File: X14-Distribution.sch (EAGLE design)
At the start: 57 parts, among them J2 PESC-02-12-02-01-X-VT-LC(DIST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, Q1 310mA/60V/1.6Ω, Q2 IRF1018EPBF, Q3 IRF1018EPBF, Q4 IRF1018EPBF, Q5 IRLML5203, Q6 IRLML5203, Q7 IRLML5203, Q8 IRLML5203, U1 DIST_OR_CONTROL_ALTMK06A-M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

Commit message: Made some more changes to the board
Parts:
- renumbered J2 to BRICKS2
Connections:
- net +12V: no longer D13.C, D14.C
- net +12V_A: now also D13.C
- net +12V_B: now also D14.C
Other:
- moved on the sheet: D13, D14
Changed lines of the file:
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@@
 <part name="CONVERSION" library="CONN, Distribution-Conversion" deviceset="DISTRIBUTION-CONVERSION" device=""/>
 <part name="BRICKS1" library="CONN, Distribution-Bricks" deviceset="PESC-02-12-02-01-X-VT-LC(DISTRIBUTION-BRICKS)" device=""/>
-<part name="J2" library="CONN, Distribution-Bricks" deviceset="PESC-02-12-02-01-X-VT-LC(DISTRIBUTION-BRICKS)" device=""/>
+<part name="BRICKS2" library="CONN, Distribution-Bricks" deviceset="PESC-02-12-02-01-X-VT-LC(DISTRIBUTION-BRICKS)" device=""/>
 <part name="D13" library="SparkFun-DiscreteSemi" library_urn="urn:adsk.eagle:library:514" deviceset="DIODE-ZENER" device="-DZ2J150M0L" package3d_urn="urn:adsk.eagle:package:38444/1" value="18V"/>
 <part name="D14" library="SparkFun-DiscreteSemi" library_urn="urn:adsk.eagle:library:514" deviceset="DIODE-ZENER" device="-DZ2J150M0L" package3d_urn="urn:adsk.eagle:package:38444/1" value="18V"/>
@@
 <attribute name="VALUE" x="76.2" y="-158.496" size="1.778" layer="96"/>
 </instance>
-<instance part="J2" gate="G$1" x="181.864" y="-140.208" smashed="yes">
+<instance part="BRICKS2" gate="G$1" x="181.864" y="-140.208" smashed="yes">
 <attribute name="NAME" x="169.164" y="-124.46" size="1.778" layer="95"/>
 <attribute name="VALUE" x="169.164" y="-157.988" size="1.778" layer="96"/>
 </instance>
-<instance part="D13" gate="G$1" x="67.564" y="133.604" smashed="yes" rot="R90">
-<attribute name="NAME" x="65.532" y="131.064" size="1.778" layer="95" font="vector" rot="R90"/>
-<attribute name="VALUE" x="69.596" y="131.064" size="1.778" layer="96" font="vector" rot="R90" align="top-left"/>
-</instance>
-<instance part="D14" gate="G$1" x="67.818" y="77.216" smashed="yes" rot="R90">
-<attribute name="NAME" x="65.786" y="74.676" size="1.778" layer="95" font="vector" rot="R90"/>
-<attribute name="VALUE" x="69.85" y="74.676" size="1.778" layer="96" font="vector" rot="R90" align="top-left"/>
+<instance part="D13" gate="G$1" x="30.988" y="136.144" smashed="yes" rot="R90">
+<attribute name="NAME" x="28.956" y="133.604" size="1.778" layer="95" font="vector" rot="R90"/>
+<attribute name="VALUE" x="33.02" y="133.604" size="1.778" layer="96" font="vector" rot="R90" align="top-left"/>
+</instance>
+<instance part="D14" gate="G$1" x="30.988" y="80.264" smashed="yes" rot="R90">
+<attribute name="NAME" x="28.956" y="77.724" size="1.778" layer="95" font="vector" rot="R90"/>
+<attribute name="VALUE" x="33.02" y="77.724" size="1.778" layer="96" font="vector" rot="R90" align="top-left"/>
 </instance>
 </instances>
@@
 <wire x1="164.084" y1="-150.368" x2="154.432" y2="-150.368" width="0.1524" layer="91"/>
 <label x="154.432" y="-150.368" size="1.778" layer="95" rot="R180" xref="yes"/>
-<pinref part="J2" gate="G$1" pin="48V_GND"/>
+<pinref part="BRICKS2" gate="G$1" pin="48V_GND"/>
 </segment>
 </net>
@@
 <wire x1="164.084" y1="-145.288" x2="154.432" y2="-145.288" width="0.1524" layer="91"/>
 <label x="154.432" y="-145.288" size="1.778" layer="95" rot="R180" xref="yes"/>
-<pinref part="J2" gate="G$1" pin="48V"/>
+<pinref part="BRICKS2" gate="G$1" pin="48V"/>
 </segment>
 </net>
@@
 <wire x1="202.184" y1="-150.368" x2="212.598" y2="-150.368" width="0.1524" layer="91"/>
 <label x="212.598" y="-150.368" size="1.778" layer="95" xref="yes"/>
-<pinref part="J2" gate="G$1" pin="ON/OFF"/>
+<pinref part="BRICKS2" gate="G$1" pin="ON/OFF"/>
 </segment>
 </net>
@@
 <pinref part="U2" gate="A" pin="IN"/>
 <wire x1="36.83" y1="85.344" x2="36.83" y2="73.66" width="0.1524" layer="91"/>
-<wire x1="36.83" y1="85.344" x2="26.67" y2="85.344" width="0.1524" layer="91"/>
+<wire x1="36.83" y1="85.344" x2="30.988" y2="85.344" width="0.1524" layer="91"/>
 <junction x="36.83" y="85.344"/>
 <label x="26.67" y="85.344" size="1.778" layer="95" rot="R180" xref="yes"/>
+<pinref part="D14" gate="G$1" pin="C"/>
+<wire x1="30.988" y1="85.344" x2="26.67" y2="85.344" width="0.1524" layer="91"/>
+<wire x1="30.988" y1="82.804" x2="30.988" y2="85.344" width="0.1524" layer="91"/>
+<junction x="30.988" y="85.344"/>
 </segment>
 <segment>
@@
 <wire x1="164.084" y1="-127.508" x2="154.432" y2="-127.508" width="0.1524" layer="91"/>
 <label x="154.178" y="-127.508" size="1.778" layer="95" rot="R180" xref="yes"/>
-<pinref part="J2" gate="G$1" pin="12V"/>
+<pinref part="BRICKS2" gate="G$1" pin="12V"/>
 </segment>
 <segment>
@@
 <pinref part="Q3" gate="G$1" pin="D"/>
 <wire x1="57.15" y1="141.478" x2="52.07" y2="141.478" width="0.1524" layer="91"/>
-<wire x1="57.15" y1="141.478" x2="67.564" y2="141.478" width="0.1524" layer="91"/>
+<wire x1="57.15" y1="141.478" x2="77.47" y2="141.478" width="0.1524" layer="91"/>
 <junction x="57.15" y="141.478"/>
-<wire x1="67.564" y1="141.478" x2="77.47" y2="141.478" width="0.1524" layer="91"/>
 <wire x1="77.47" y1="141.478" x2="77.47" y2="110.49" width="0.1524" layer="91"/>
 <pinref part="C1" gate="G$1" pin="+"/>
@@
 <pinref part="Q4" gate="G$1" pin="D"/>
 <wire x1="57.15" y1="85.344" x2="52.07" y2="85.344" width="0.1524" layer="91"/>
-<wire x1="57.15" y1="85.344" x2="67.818" y2="85.344" width="0.1524" layer="91"/>
+<wire x1="57.15" y1="85.344" x2="77.47" y2="85.344" width="0.1524" layer="91"/>
 <junction x="57.15" y="85.344"/>
 <junction x="77.47" y="85.344"/>
 <pinref part="U1" gate="A" pin="VS"/>
-<wire x1="67.818" y1="85.344" x2="77.47" y2="85.344" width="0.1524" layer="91"/>
 <wire x1="77.47" y1="110.49" x2="59.69" y2="110.49" width="0.1524" layer="91"/>
 <junction x="77.47" y="110.49"/>
 <pinref part="U1" gate="A" pin="OUT"/>
 <wire x1="52.07" y1="125.73" x2="57.15" y2="125.73" width="0.1524" layer="91"/>
-<pinref part="D14" gate="G$1" pin="C"/>
-<wire x1="67.818" y1="79.756" x2="67.818" y2="85.344" width="0.1524" layer="91"/>
-<junction x="67.818" y="85.344"/>
-<pinref part="D13" gate="G$1" pin="C"/>
-<wire x1="67.564" y1="136.144" x2="67.564" y2="141.478" width="0.1524" layer="91"/>
-<junction x="67.564" y="141.478"/>
 </segment>
 <segment>
@@
 <wire x1="164.084" y1="-132.588" x2="154.686" y2="-132.588" width="0.1524" layer="91"/>
 <label x="154.432" y="-132.588" size="1.778" layer="95" rot="R180" xref="yes"/>
-<pinref part="J2" gate="G$1" pin="12V_GND"/>
+<pinref part="BRICKS2" gate="G$1" pin="12V_GND"/>
 </segment>
 <segment>
@@
 <segment>
 <pinref part="D13" gate="G$1" pin="A"/>
-<wire x1="67.564" y1="131.064" x2="67.564" y2="122.174" width="0.1524" layer="91"/>
-<label x="67.31" y="122.174" size="1.27" layer="95" rot="R180" xref="yes"/>
+<wire x1="30.988" y1="133.604" x2="30.988" y2="124.714" width="0.1524" layer="91"/>
+<label x="30.734" y="124.714" size="1.27" layer="95" rot="R180" xref="yes"/>
 </segment>
 <segment>
 <pinref part="D14" gate="G$1" pin="A"/>
-<wire x1="67.818" y1="74.676" x2="67.818" y2="69.342" width="0.1524" layer="91"/>
-<label x="67.818" y="69.596" size="1.27" layer="95" rot="R180" xref="yes"/>
+<wire x1="30.988" y1="77.724" x2="30.988" y2="72.39" width="0.1524" layer="91"/>
+<label x="30.988" y="72.644" size="1.27" layer="95" rot="R180" xref="yes"/>
 </segment>
 </net>
@@
 <pinref part="Q3" gate="G$1" pin="S"/>
 <wire x1="36.83" y1="141.478" x2="41.91" y2="141.478" width="0.1524" layer="91"/>
-<wire x1="36.83" y1="141.478" x2="26.67" y2="141.478" width="0.1524" layer="91"/>
+<wire x1="36.83" y1="141.478" x2="30.988" y2="141.478" width="0.1524" layer="91"/>
 <junction x="36.83" y="141.478"/>
 <label x="26.67" y="141.478" size="1.778" layer="95" rot="MR0" xref="yes"/>
+<pinref part="D13" gate="G$1" pin="C"/>
+<wire x1="30.988" y1="141.478" x2="26.67" y2="141.478" width="0.1524" layer="91"/>
+<wire x1="30.988" y1="138.684" x2="30.988" y2="141.478" width="0.1524" layer="91"/>
+<junction x="30.988" y="141.478"/>
 </segment>
 <segment>
@@
 <wire x1="202.184" y1="-130.048" x2="212.598" y2="-130.048" width="0.1524" layer="91"/>
 <label x="212.344" y="-129.794" size="1.778" layer="95" xref="yes"/>
-<pinref part="J2" gate="G$1" pin="DATA"/>
+<pinref part="BRICKS2" gate="G$1" pin="DATA"/>
 </segment>
 </net>
@@
 <wire x1="202.184" y1="-140.208" x2="212.598" y2="-140.208" width="0.1524" layer="91"/>
 <label x="212.598" y="-140.208" size="1.778" layer="95" xref="yes"/>
-<pinref part="J2" gate="G$1" pin="CLK"/>
+<pinref part="BRICKS2" gate="G$1" pin="CLK"/>
 </segment>
 </net>
@@
 <wire x1="202.184" y1="-135.128" x2="212.598" y2="-135.128" width="0.1524" layer="91"/>
 <label x="212.09" y="-135.128" size="1.778" layer="95" xref="yes"/>
-<pinref part="J2" gate="G$1" pin="ALERT"/>
+<pinref part="BRICKS2" gate="G$1" pin="ALERT"/>
 </segment>
 </net>
@@
 <wire x1="202.184" y1="-145.288" x2="212.598" y2="-145.288" width="0.1524" layer="91"/>
 <label x="212.598" y="-145.288" size="1.778" layer="95" xref="yes"/>
-<pinref part="J2" gate="G$1" pin="C2"/>
-</segment>
-</net>
+<pinref part="BRICKS2" gate="G$1" pin="C2"/>
+</segment>
+</net>

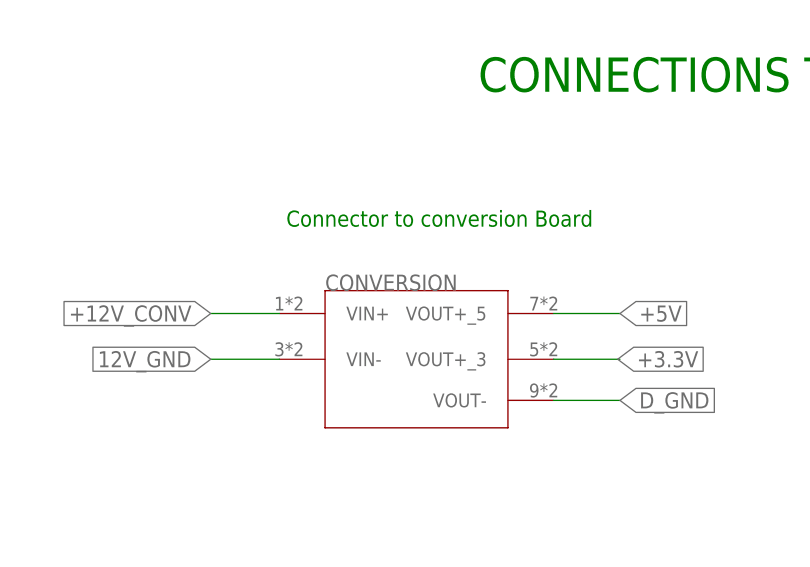
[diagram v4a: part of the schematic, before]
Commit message: Length-matched the DATA and CLK lines
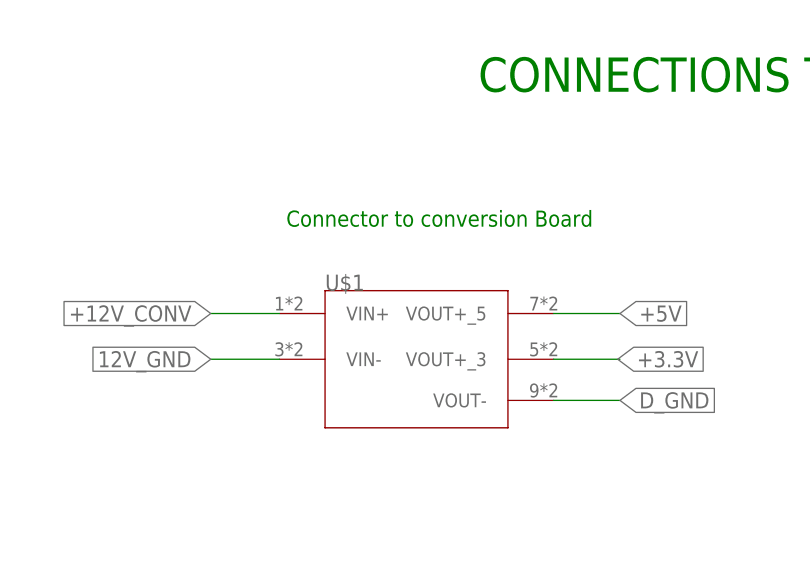
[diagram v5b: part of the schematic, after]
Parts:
- renumbered CONVERSION to U$1
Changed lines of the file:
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@@
 <part name="TETHER_POSITIVE" library="CONN, 3 pin connection to tether" deviceset="796636-3" device=""/>
 <part name="TETHER_GND" library="CONN, 3 pin connection to tether" deviceset="796636-3" device=""/>
-<part name="CONVERSION" library="CONN, Distribution-Conversion" deviceset="DISTRIBUTION-CONVERSION" device=""/>
 <part name="BRICKS1" library="CONN, Distribution-Bricks" deviceset="PESC-02-12-02-01-X-VT-LC(DISTRIBUTION-BRICKS)" device=""/>
 <part name="BRICKS2" library="CONN, Distribution-Bricks" deviceset="PESC-02-12-02-01-X-VT-LC(DISTRIBUTION-BRICKS)" device=""/>
 <part name="D13" library="SparkFun-DiscreteSemi" library_urn="urn:adsk.eagle:library:514" deviceset="DIODE-ZENER" device="-DZ2J150M0L" package3d_urn="urn:adsk.eagle:package:38444/1" value="18V"/>
 <part name="D14" library="SparkFun-DiscreteSemi" library_urn="urn:adsk.eagle:library:514" deviceset="DIODE-ZENER" device="-DZ2J150M0L" package3d_urn="urn:adsk.eagle:package:38444/1" value="18V"/>
+<part name="U$1" library="CONN, Distribution-Conversion" deviceset="DISTRIBUTION-CONVERSION" device=""/>
 </parts>
 <sheets>
@@
 <attribute name="NAME" x="377.698" y="-55.118" size="1.778" layer="95"/>
 </instance>
-<instance part="CONVERSION" gate="G$1" x="86.868" y="-61.722" smashed="yes">
-<attribute name="NAME" x="79.248" y="-54.102" size="1.778" layer="95"/>
-</instance>
 <instance part="BRICKS1" gate="G$1" x="88.9" y="-140.716" smashed="yes">
 <attribute name="NAME" x="76.2" y="-124.968" size="1.778" layer="95"/>
@@
 <attribute name="NAME" x="28.956" y="77.724" size="1.778" layer="95" font="vector" rot="R90"/>
 <attribute name="VALUE" x="33.02" y="77.724" size="1.778" layer="96" font="vector" rot="R90" align="top-left"/>
+</instance>
+<instance part="U$1" gate="G$1" x="86.868" y="-61.722" smashed="yes">
+<attribute name="NAME" x="79.248" y="-54.102" size="1.778" layer="95"/>
 </instance>
 </instances>
@@
 <wire x1="74.168" y1="-61.722" x2="66.548" y2="-61.722" width="0.1524" layer="91"/>
 <label x="66.548" y="-61.722" size="1.778" layer="95" rot="R180" xref="yes"/>
-<pinref part="CONVERSION" gate="G$1" pin="VIN-"/>
+<pinref part="U$1" gate="G$1" pin="VIN-"/>
 </segment>
 <segment>
@@
 <wire x1="74.168" y1="-56.642" x2="66.548" y2="-56.642" width="0.1524" layer="91"/>
 <label x="66.548" y="-56.642" size="1.778" layer="95" rot="R180" xref="yes"/>
-<pinref part="CONVERSION" gate="G$1" pin="VIN+"/>
+<pinref part="U$1" gate="G$1" pin="VIN+"/>
 </segment>
 <segment>
@@
 <wire x1="104.648" y1="-56.642" x2="112.014" y2="-56.642" width="0.1524" layer="91"/>
 <label x="112.014" y="-56.642" size="1.778" layer="95" xref="yes"/>
-<pinref part="CONVERSION" gate="G$1" pin="VOUT+_5"/>
+<pinref part="U$1" gate="G$1" pin="VOUT+_5"/>
 </segment>
 </net>
@@
 <wire x1="104.648" y1="-61.722" x2="112.014" y2="-61.722" width="0.1524" layer="91"/>
 <label x="111.76" y="-61.722" size="1.778" layer="95" xref="yes"/>
-<pinref part="CONVERSION" gate="G$1" pin="VOUT+_3"/>
+<pinref part="U$1" gate="G$1" pin="VOUT+_3"/>
 </segment>
 </net>
@@
 <wire x1="104.648" y1="-66.294" x2="112.014" y2="-66.294" width="0.1524" layer="91"/>
 <label x="112.014" y="-66.294" size="1.778" layer="95" xref="yes"/>
-<pinref part="CONVERSION" gate="G$1" pin="VOUT-"/>
-</segment>
-<segment>
+<pinref part="U$1" gate="G$1" pin="VOUT-"/>
+</segment>
+<segment>
